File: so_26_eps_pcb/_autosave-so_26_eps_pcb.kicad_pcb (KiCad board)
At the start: 4 copper layers, 90.2 x 95.9 mm, 47 parts, among them J1 Conn_02x12_Odd_Even, J3 Conn_01x02, SW1 SW_SPDT, U1 LM22679TJ-ADJ/NOPB, U2 LM22679TJ-ADJ/NOPB

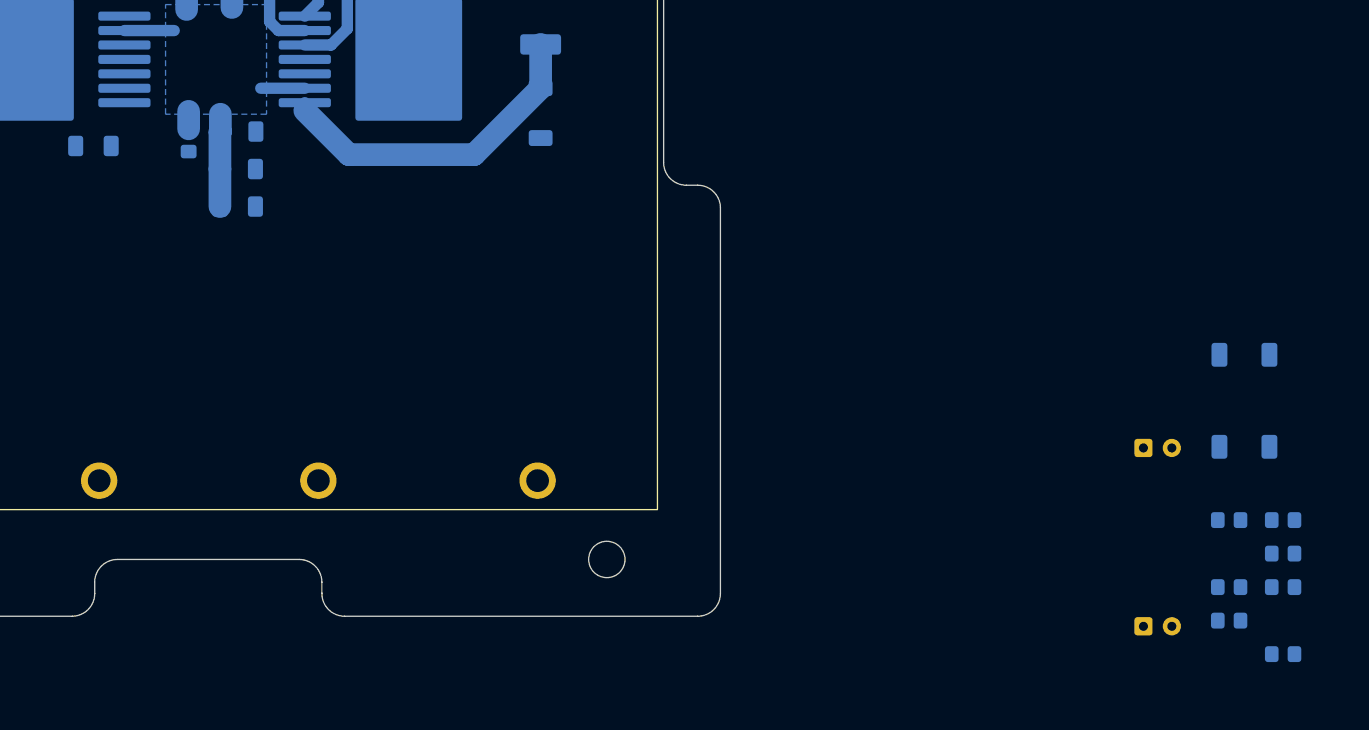
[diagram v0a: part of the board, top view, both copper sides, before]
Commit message: Tried to make a design of the 10V reg and started on the 3V3 reg
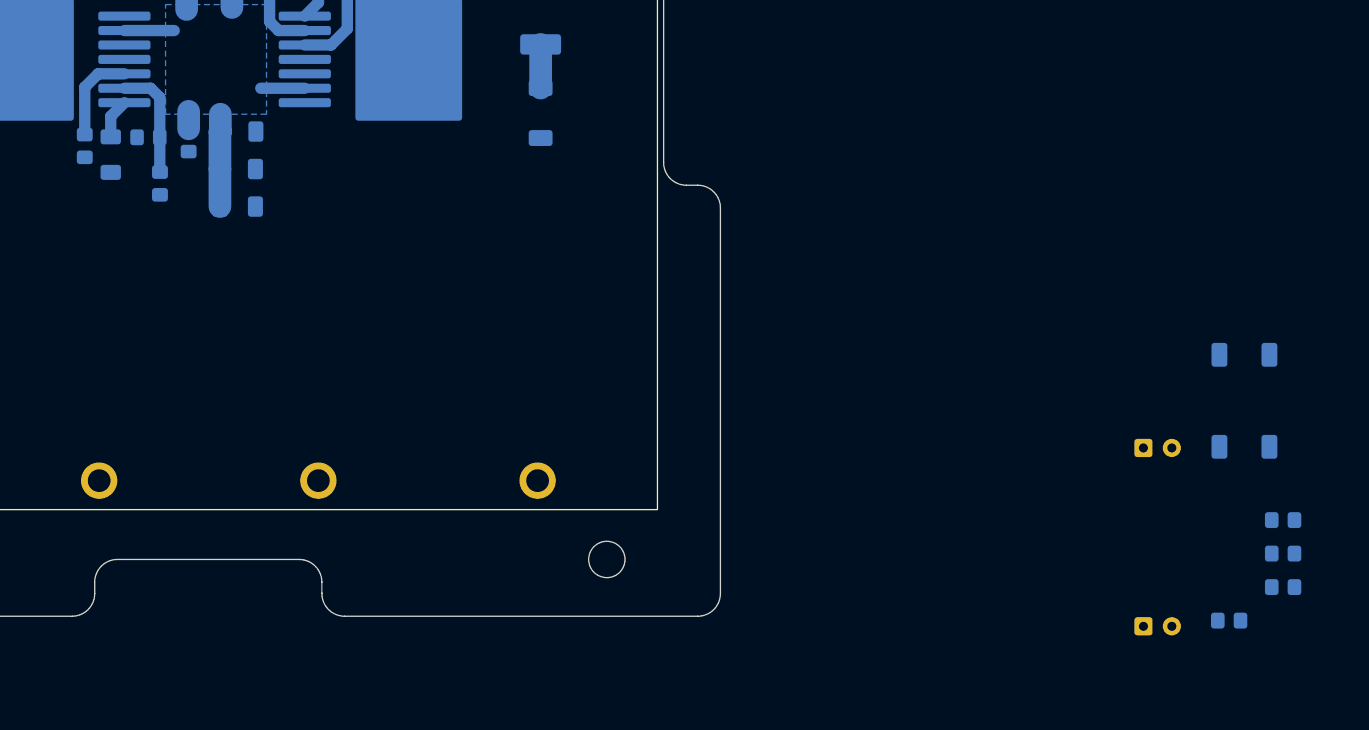
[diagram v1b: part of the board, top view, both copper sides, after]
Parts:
- moved R3 108.0 mm to (97.8, 77.8), turned to -90 degrees
- moved R7 107.2 mm to (104.4, 81.1), turned to -90 degrees
- moved R5 100.9 mm to (103.4, 77.0), turned to 180 degrees
- moved C7 1.70 mm to (100.1, 78.6), turned to 90 degrees
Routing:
- net Net-(D2-K): track 29.3 -> 3.84 mm
- net Net-(U1-FB): track 0.00 -> 10.0 mm
- net Net-(U1-IADJ): track 0.00 -> 8.15 mm
- net Net-(U1-SS): track 0.00 -> 3.51 mm
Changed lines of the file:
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@@
 	(footprint "Resistor_SMD:R_0805_2012Metric_Pad1.20x1.40mm_HandSolder"
 		(layer "B.Cu")
-		(at 198.536 116.629)
+		(at 97.79 77.793 -90)
 		(descr "Resistor SMD 0805 (2012 Metric), square (rectangular) end terminal, IPC-7351 nominal with elongated pad for handsoldering. (Body size source: IPC-SM-782 page 72, https://www.pcb-3d.com/wordpress/wp-content/uploads/ipc-sm-782a_amendment_1_and_2.pdf), generated with kicad-footprint-generator")
 		(tags "resistor handsolder")
 		(property "Reference" "R3"
-			(at 0 1.65 180)
+			(at 0 1.65 90)
 			(layer "B.SilkS")
 			(effects
@@
 		)
 		(property "Value" "R_Small"
-			(at 0 -1.65 180)
+			(at 0 -1.65 90)
 			(layer "B.Fab")
 			(effects
@@
 		)
 		(property "Datasheet" "~"
-			(at 0 0 180)
+			(at 0 0 90)
 			(layer "B.Fab")
 			(hide yes)
@@
 		)
 		(property "Description" "Resistor, small symbol"
-			(at 0 0 180)
+			(at 0 0 90)
 			(layer "B.Fab")
 			(hide yes)
@@
 		(attr smd)
 		(fp_line
-			(start -0.227064 -0.735)
-			(end 0.227064 -0.735)
+			(start -0.227064 0.735)
+			(end 0.227064 0.735)
 			(stroke
 				(width 0.12)
@@
 		)
 		(fp_line
-			(start -0.227064 0.735)
-			(end 0.227064 0.735)
+			(start -0.227064 -0.735)
+			(end 0.227064 -0.735)
 			(stroke
 				(width 0.12)
@@
 		)
 		(fp_text user "${REFERENCE}"
-			(at 0 0 180)
+			(at 0 0 90)
 			(layer "B.Fab")
 			(effects
@@
 		)
 		(pad "1" smd roundrect
-			(at -1 0)
+			(at -1 0 270)
 			(size 1.2 1.4)
 			(layers "B.Cu" "B.Mask" "B.Paste")
@@
 		)
 		(pad "2" smd roundrect
-			(at 1 0)
+			(at 1 0 270)
 			(size 1.2 1.4)
 			(layers "B.Cu" "B.Mask" "B.Paste")
@@
 	(footprint "Capacitor_SMD:C_1206_3216Metric_Pad1.33x1.80mm_HandSolder"
 		(layer "B.Cu")
-		(at 98.552 77.793 180)
+		(at 100.076 78.555 90)
 		(descr "Capacitor SMD 1206 (3216 Metric), square (rectangular) end terminal, IPC-7351 nominal with elongated pad for handsoldering. (Body size source: IPC-SM-782 page 76, https://www.pcb-3d.com/wordpress/wp-content/uploads/ipc-sm-782a_amendment_1_and_2.pdf), generated with kicad-footprint-generator")
 		(tags "capacitor handsolder")
 		(property "Reference" "C7"
-			(at 0 1.85 0)
+			(at 0 1.85 90)
 			(layer "B.SilkS")
 			(effects
@@
 		)
 		(property "Value" "1 uF"
-			(at 0 -1.85 0)
+			(at 0 -1.85 90)
 			(layer "B.Fab")
 			(effects
@@
 		)
 		(property "Datasheet" "~"
-			(at 0 0 0)
+			(at 0 0 90)
 			(layer "B.Fab")
 			(hide yes)
@@
 		)
 		(property "Description" "Unpolarized capacitor, small symbol"
-			(at 0 0 0)
+			(at 0 0 90)
 			(layer "B.Fab")
 			(hide yes)
@@
 		(attr smd)
 		(fp_line
-			(start -0.711252 0.91)
-			(end 0.711252 0.91)
+			(start -0.711252 -0.91)
+			(end 0.711252 -0.91)
 			(stroke
 				(width 0.12)
@@
 		)
 		(fp_line
-			(start -0.711252 -0.91)
-			(end 0.711252 -0.91)
+			(start -0.711252 0.91)
+			(end 0.711252 0.91)
 			(stroke
 				(width 0.12)
@@
 		)
 		(fp_text user "${REFERENCE}"
-			(at 0 0 0)
+			(at 0 0 90)
 			(layer "B.Fab")
 			(effects
@@
 		)
 		(pad "1" smd roundrect
-			(at -1.5625 0 180)
+			(at -1.5625 0 90)
 			(size 1.325 1.8)
 			(layers "B.Cu" "B.Mask" "B.Paste")
@@
 		)
 		(pad "2" smd roundrect
-			(at 1.5625 0 180)
+			(at 1.5625 0 90)
 			(size 1.325 1.8)
 			(layers "B.Cu" "B.Mask" "B.Paste")
@@
 	(footprint "Resistor_SMD:R_0805_2012Metric_Pad1.20x1.40mm_HandSolder"
 		(layer "B.Cu")
-		(at 203.286 122.529)
+		(at 104.41 81.095 -90)
 		(descr "Resistor SMD 0805 (2012 Metric), square (rectangular) end terminal, IPC-7351 nominal with elongated pad for handsoldering. (Body size source: IPC-SM-782 page 72, https://www.pcb-3d.com/wordpress/wp-content/uploads/ipc-sm-782a_amendment_1_and_2.pdf), generated with kicad-footprint-generator")
 		(tags "resistor handsolder")
 		(property "Reference" "R7"
-			(at 0 1.65 180)
+			(at 0 1.65 90)
 			(layer "B.SilkS")
 			(effects
@@
 		)
 		(property "Value" "1kohm"
-			(at 0 -1.65 180)
+			(at 0 -1.65 90)
 			(layer "B.Fab")
 			(effects
@@
 		)
 		(property "Datasheet" "~"
-			(at 0 0 180)
+			(at 0 0 90)
 			(layer "B.Fab")
 			(hide yes)
@@
 		)
 		(property "Description" "Resistor, small symbol"
-			(at 0 0 180)
+			(at 0 0 90)
 			(layer "B.Fab")
 			(hide yes)
@@
 		(attr smd)
 		(fp_line
-			(start -0.227064 -0.735)
-			(end 0.227064 -0.735)
+			(start -0.227064 0.735)
+			(end 0.227064 0.735)
 			(stroke
 				(width 0.12)
@@
 		)
 		(fp_line
-			(start -0.227064 0.735)
-			(end 0.227064 0.735)
+			(start -0.227064 -0.735)
+			(end 0.227064 -0.735)
 			(stroke
 				(width 0.12)
@@
 		)
 		(fp_text user "${REFERENCE}"
-			(at 0 0 180)
+			(at 0 0 90)
 			(layer "B.Fab")
 			(effects
@@
 		)
 		(pad "1" smd roundrect
-			(at -1 0)
+			(at -1 0 270)
 			(size 1.2 1.4)
 			(layers "B.Cu" "B.Mask" "B.Paste")
@@
 		)
 		(pad "2" smd roundrect
-			(at 1 0)
+			(at 1 0 270)
 			(size 1.2 1.4)
 			(layers "B.Cu" "B.Mask" "B.Paste")
@@
 	(footprint "Resistor_SMD:R_0805_2012Metric_Pad1.20x1.40mm_HandSolder"
 		(layer "B.Cu")
-		(at 198.536 110.729)
+		(at 103.394 77.031 180)
 		(descr "Resistor SMD 0805 (2012 Metric), square (rectangular) end terminal, IPC-7351 nominal with elongated pad for handsoldering. (Body size source: IPC-SM-782 page 72, https://www.pcb-3d.com/wordpress/wp-content/uploads/ipc-sm-782a_amendment_1_and_2.pdf), generated with kicad-footprint-generator")
 		(tags "resistor handsolder")
 		(property "Reference" "R5"
-			(at 0 1.65 180)
+			(at 0 1.65 0)
 			(layer "B.SilkS")
 			(effects
@@
 		)
 		(property "Value" "1,6kohm"
-			(at 0 -1.65 180)
+			(at 0 -1.65 0)
 			(layer "B.Fab")
 			(effects
@@
 		)
 		(property "Datasheet" "~"
-			(at 0 0 180)
+			(at 0 0 0)
 			(layer "B.Fab")
 			(hide yes)
@@
 		)
 		(property "Description" "Resistor, small symbol"
-			(at 0 0 180)
+			(at 0 0 0)
 			(layer "B.Fab")
 			(hide yes)
@@
 		(attr smd)
 		(fp_line
-			(start -0.227064 -0.735)
-			(end 0.227064 -0.735)
+			(start -0.227064 0.735)
+			(end 0.227064 0.735)
 			(stroke
 				(width 0.12)
@@
 		)
 		(fp_line
-			(start -0.227064 0.735)
-			(end 0.227064 0.735)
+			(start -0.227064 -0.735)
+			(end 0.227064 -0.735)
 			(stroke
 				(width 0.12)
@@
 		)
 		(fp_text user "${REFERENCE}"
-			(at 0 0 180)
+			(at 0 0 0)
 			(layer "B.Fab")
 			(effects
@@
 		)
 		(pad "1" smd roundrect
-			(at -1 0)
+			(at -1 0 180)
 			(size 1.2 1.4)
 			(layers "B.Cu" "B.Mask" "B.Paste")
@@
 		)
 		(pad "2" smd roundrect
-			(at 1 0)
+			(at 1 0 180)
 			(size 1.2 1.4)
 			(layers "B.Cu" "B.Mask" "B.Paste")
@@
 	)
 	(segment
-		(start 118.364 63.6075)
-		(end 118.364 65.16)
+		(start 100.076 76.9925)
+		(end 100.076 75.186)
 		(width 1)
 		(layer "B.Cu")
-		(net 4)
+		(net 3)
 	)
 	(segment
-		(start 118.364 65.16)
-		(end 117.161 66.363)
+		(start 100.076 75.186)
+		(end 101.279 73.983)
 		(width 1)
 		(layer "B.Cu")
-		(net 4)
-	)
-	(segment
-		(start 121.038 78.555)
-		(end 132.062322 78.555)
-		(width 2)
-		(layer "B.Cu")
-		(net 8)
+		(net 3)
 	)
 	(segment
-		(start 132.062322 78.555)
-		(end 137.922 72.695322)
-		(width 2)
+		(start 118.364 63.6075)
+		(end 118.364 65.16)
+		(width 1)
 		(layer "B.Cu")
-		(net 8)
+		(net 4)
 	)
 	(segment
-		(start 117.161 74.678)
-		(end 121.038 78.555)
-		(width 2)
+		(start 118.364 65.16)
+		(end 117.161 66.363)
+		(width 1)
 		(layer "B.Cu")
-		(net 8)
+		(net 4)
 	)
 	(segment
@@
 	)
 	(segment
-		(start 117.161 73.983)
-		(end 117.161 74.678)
-		(width 1)
-		(layer "B.Cu")
-		(net 8)
-	)
-	(segment
 		(start 137.922 59.854322)
 		(end 137.922 57.369322)
@@
 	)
 	(segment
+		(start 97.79 76.793)
+		(end 97.79 72.622252)
+		(width 1)
+		(layer "B.Cu")
+		(net 20)
+	)
+	(segment
+		(start 97.79 72.622252)
+		(end 98.969252 71.443)
+		(width 1)
+		(layer "B.Cu")
+		(net 20)
+	)
+	(segment
+		(start 98.969252 71.443)
+		(end 101.279 71.443)
+		(width 1)
+		(layer "B.Cu")
+		(net 20)
+	)
+	(segment
 		(start 119.470748 68.903)
 		(end 117.161 68.903)
@@
 	)
 	(segment
+		(start 104.394 73.518252)
+		(end 103.588748 72.713)
+		(width 1)
+		(layer "B.Cu")
+		(net 22)
+	)
+	(segment
+		(start 104.394 80.079)
+		(end 104.41 80.095)
+		(width 1)
+		(layer "B.Cu")
+		(net 22)
+	)
+	(segment
+		(start 104.394 77.031)
+		(end 104.394 80.079)
+		(width 1)
+		(layer "B.Cu")
+		(net 22)
+	)
+	(segment
+		(start 104.394 77.031)
+		(end 104.394 73.518252)
+		(width 1)
+		(layer "B.Cu")
+		(net 22)
+	)
+	(segment
+		(start 103.588748 72.713)
+		(end 101.279 72.713)
+		(width 1)
+		(layer "B.Cu")
+		(net 22)
+	)
+	(segment
